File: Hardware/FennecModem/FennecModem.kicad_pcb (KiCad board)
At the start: 4 copper layers, 75 x 116.7 mm, 70 parts, among them J1 Conn_02x04_Odd_Even, J201 Conn_Coaxial, J3 Conn_02x04_Odd_Even, M1 Fan, Q2 AO3401A, Q3 MMBT3906, Q801 MMBT3904, U1 MCP6022, U2 L7805, U201 DRA818V, U4 SN74LVC245APW

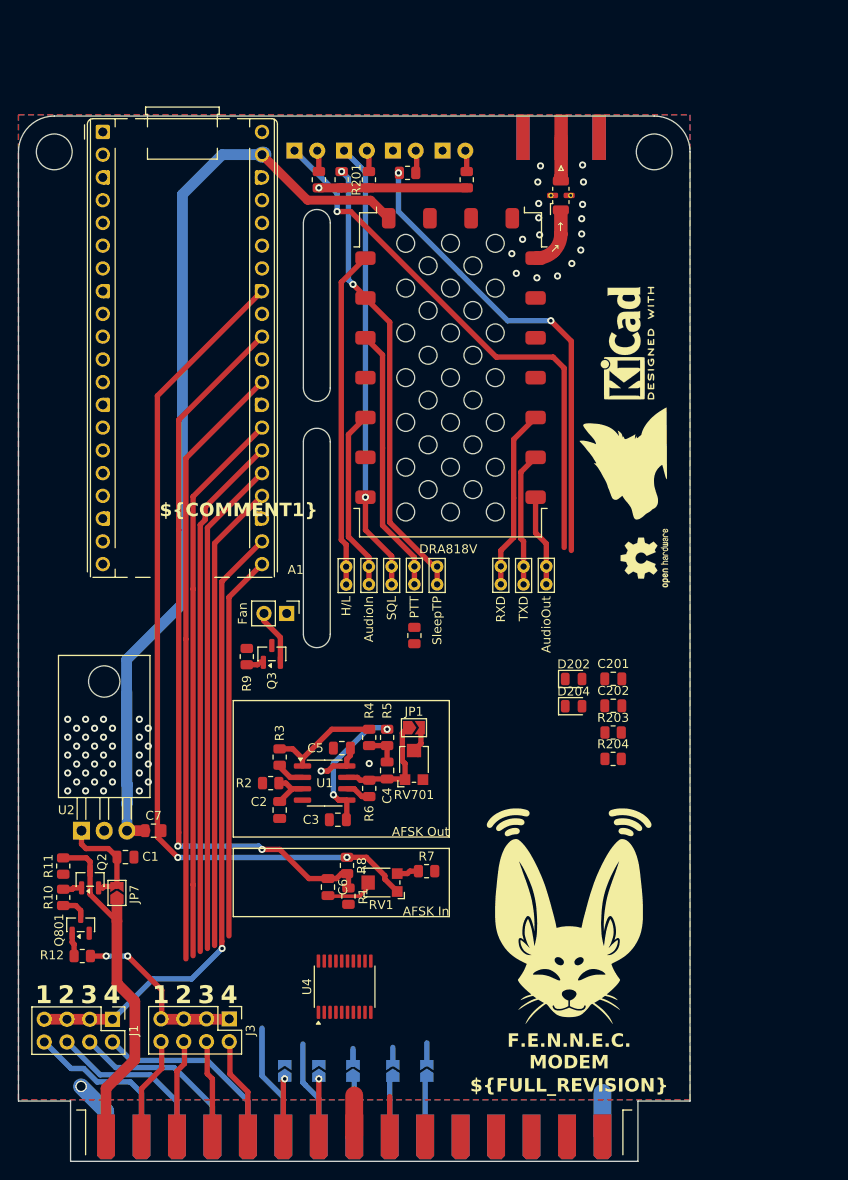
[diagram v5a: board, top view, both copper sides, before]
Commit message: Add all nets
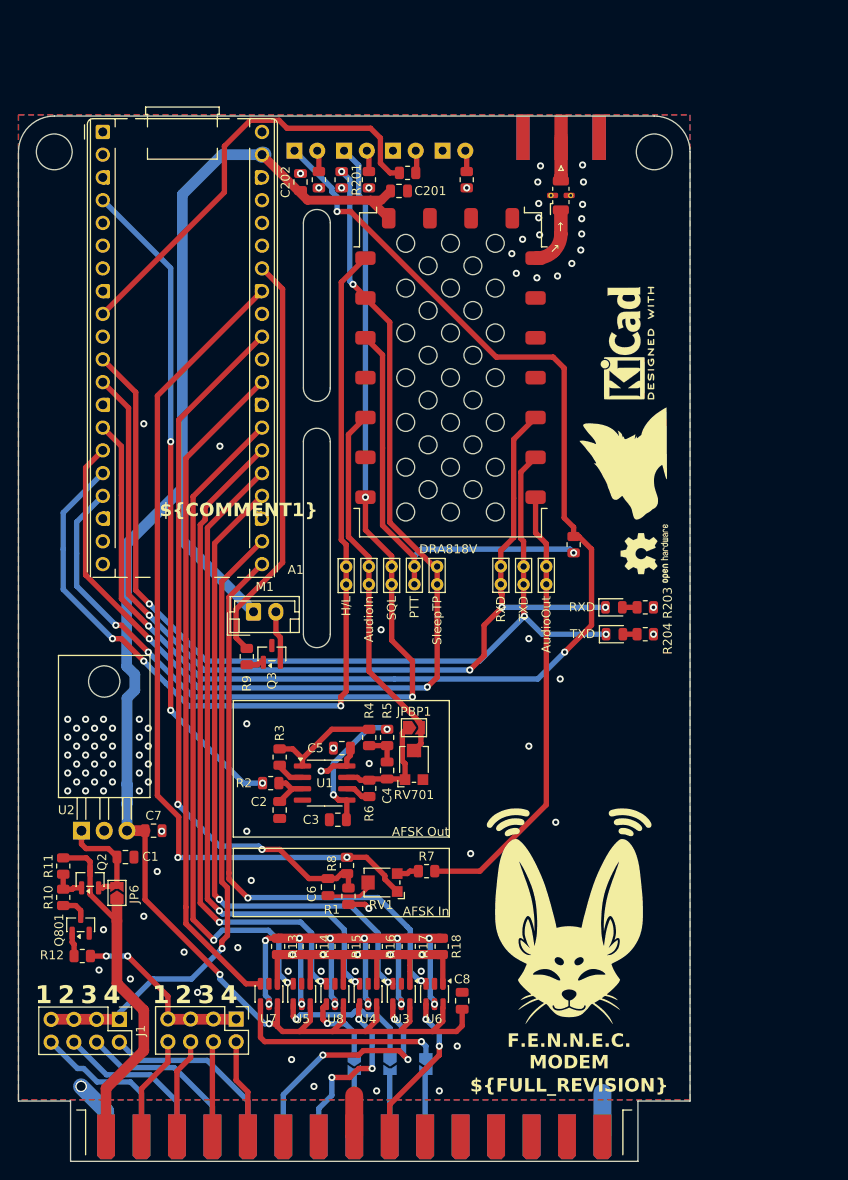
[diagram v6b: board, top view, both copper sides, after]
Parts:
- removed JP2: SolderJumper_2_Open, Jumper:SolderJumper-2_P1.3mm_Open_TrianglePad1.0x1.5mm
- removed the JP6 at (158.1, 146.8)
- added C8: 0.1μf, Capacitor_SMD:C_0805_2012Metric, F.Cu at (162.1, 138.9)
- added R13: 100K, Resistor_SMD:R_0805_2012Metric, F.Cu at (141.5, 132.9)
- added R14: 100K, Resistor_SMD:R_0805_2012Metric, F.Cu at (145.0, 132.9)
- added R15: 100K, Resistor_SMD:R_0805_2012Metric, F.Cu at (148.6, 132.9)
- added R16: 100K, Resistor_SMD:R_0805_2012Metric, F.Cu at (152.4, 132.9)
- added R17: 100K, Resistor_SMD:R_0805_2012Metric, F.Cu at (156.1, 132.9)
- added R18: 100K, Resistor_SMD:R_0805_2012Metric, F.Cu at (159.8, 132.9)
- added U3: SN74LVC1T45DBV, Package_TO_SOT_SMD:SOT-23-6, F.Cu at (155.3, 138.2)
- added U5: SN74LVC1T45DBV, Package_TO_SOT_SMD:SOT-23-6, F.Cu at (144.1, 138.2)
- added U6: SN74LVC1T45DBV, Package_TO_SOT_SMD:SOT-23-6, F.Cu at (159.0, 138.2)
- added U7: SN74LVC1T45DBV, Package_TO_SOT_SMD:SOT-23-6, F.Cu at (140.5, 138.2)
- added U8: SN74LVC1T45DBV, Package_TO_SOT_SMD:SOT-23-6, F.Cu at (147.8, 138.2)
- J1: value Conn_02x04_Odd_Even -> SEL_ADDR
- J3: value Conn_02x04_Odd_Even -> EN_ADDR
- M1: footprint Connector_PinHeader_2.54mm:PinHeader_1x02_P2.54mm_Vertical -> Connector_JST:JST_EH_B2B-EH-A_1x02_P2.50mm_Vertical
- U4: value SN74LVC245APW -> SN74LVC1T45DBV; footprint Package_SO:TSSOP-20_4.4x6.5mm_P0.65mm -> Package_TO_SOT_SMD:SOT-23-6
- moved C202 68.1 mm to (144.0, 47.5), turned to 90 degrees
- moved C201 59.5 mm to (155.0, 48.5)
- moved R206 20.5 mm to (174.5, 88.0), turned to -90 degrees
- moved R203 14.4 mm to (182.5, 95.0)
- moved R204 14.4 mm to (182.5, 98.0)
- moved D204 9.24 mm to (179.1, 98.0)
- moved D202 9.18 mm to (179.0, 95.0)
- moved JP4 4.21 mm to (154.0, 146.0), turned to -90 degrees
- moved JP3 4.03 mm to (150.0, 146.0), turned to -90 degrees
- moved JP5 3.78 mm to (158.0, 146.0), turned to -90 degrees
- moved M1 3.71 mm to (138.8, 95.5), turned to 0 degrees
- moved U4 2.75 mm to (151.6, 138.2), turned to -90 degrees
- moved J3 0.77 mm to (136.8, 141.0)
- moved J1 0.77 mm to (123.8, 141.0)
- moved REF** 0.50 mm to (182.5, 89.0)
- renumbered JP7 to JP6, JP1 to JPBP1
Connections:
- A1 pad 26: Net-(A1-GPIO20) -> /SPI2
- A1 pad 27: Net-(A1-GPIO21) -> /SPI3
- A1 pad 29: Net-(A1-GPIO22) -> /SPI4
- A1 pad 6: Net-(A1-GPIO4) -> /SDA
- A1 pad 7: Net-(A1-GPIO5) -> /SCL
- JP3 pad 1: /SDA -> /Backplane/_SPI_SDA2
- JP3 pad 2: Net-(A1-GPIO4) -> Net-(JP3-B)
- JP4 pad 1: /SPI2 -> /Backplane/_SPI_SDA3
- JP4 pad 2: Net-(A1-GPIO20) -> Net-(JP4-B)
- JP5 pad 1: /SPI3 -> /Backplane/_SPI_SDA4
- JP5 pad 2: Net-(A1-GPIO21) -> Net-(JP5-B)
- U302 pad 11: /SCL -> unconnected-(U302-I2C_SCL-Pad11)
- U302 pad 12: /SPI_CLK -> /Backplane/_SPI_CLK
- U302 pad 13: /SDA -> unconnected-(U302-I2C_SDA-Pad13)
- U302 pad 14: /SDI -> /Backplane/_SPI_SDA1
- U302 pad 16: /SPI2 -> Net-(JP3-B)
- U302 pad 17: /SDO -> /Backplane/_SPI_SDO
- U302 pad 18: /SPI3 -> Net-(JP4-B)
- U302 pad 20: /SPI4 -> Net-(JP5-B)
- U4 pad 1: unconnected-(U4-DIR-Pad1) -> +3.3V
- U4 pad 2: unconnected-(U4-A1-Pad2) -> GND
- U4 pad 3: unconnected-(U4-A2-Pad3) -> /SDI
- U4 pad 4: unconnected-(U4-A3-Pad4) -> /Backplane/_SPI_SDA1
- U4 pad 5: unconnected-(U4-A4-Pad5) -> /Backplane/DIR
- U4 pad 6: unconnected-(U4-A5-Pad6) -> +5V
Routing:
- net /RXD: track 15.0 -> 104.6 mm, vias 0 -> 3
- net /TXD: track 20.2 -> 109.4 mm, vias 0 -> 4
- net /PTT: track 61.4 -> 150.4 mm, vias 1 -> 3
- net +5V: track 116.2 -> 196.7 mm, vias 0 -> 2
- net /TONE_OUT: track 0.00 -> 73.7 mm, vias 0 -> 3
- net Net-(A1-GPIO22): track 70.3 -> 0.00 mm
- net /Sleep: track 50.7 -> 120.8 mm, vias 2 -> 4
- net /SPI3: track 6.78 -> 75.4 mm, vias 0 -> 2
- net /SPI4: track 6.72 -> 75.1 mm
- net /SQL: track 50.6 -> 118.1 mm, vias 1 -> 4
- net /SPI2: track 6.69 -> 73.9 mm, vias 0 -> 2
- net /Backplane/DIR: track 0.00 -> 67.0 mm, vias 0 -> 12
- net /H/L: track 37.8 -> 102.8 mm, vias 0 -> 3
- net Net-(A1-GPIO21): track 64.0 -> 0.00 mm
- net Net-(A1-GPIO20): track 60.6 -> 0.00 mm
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
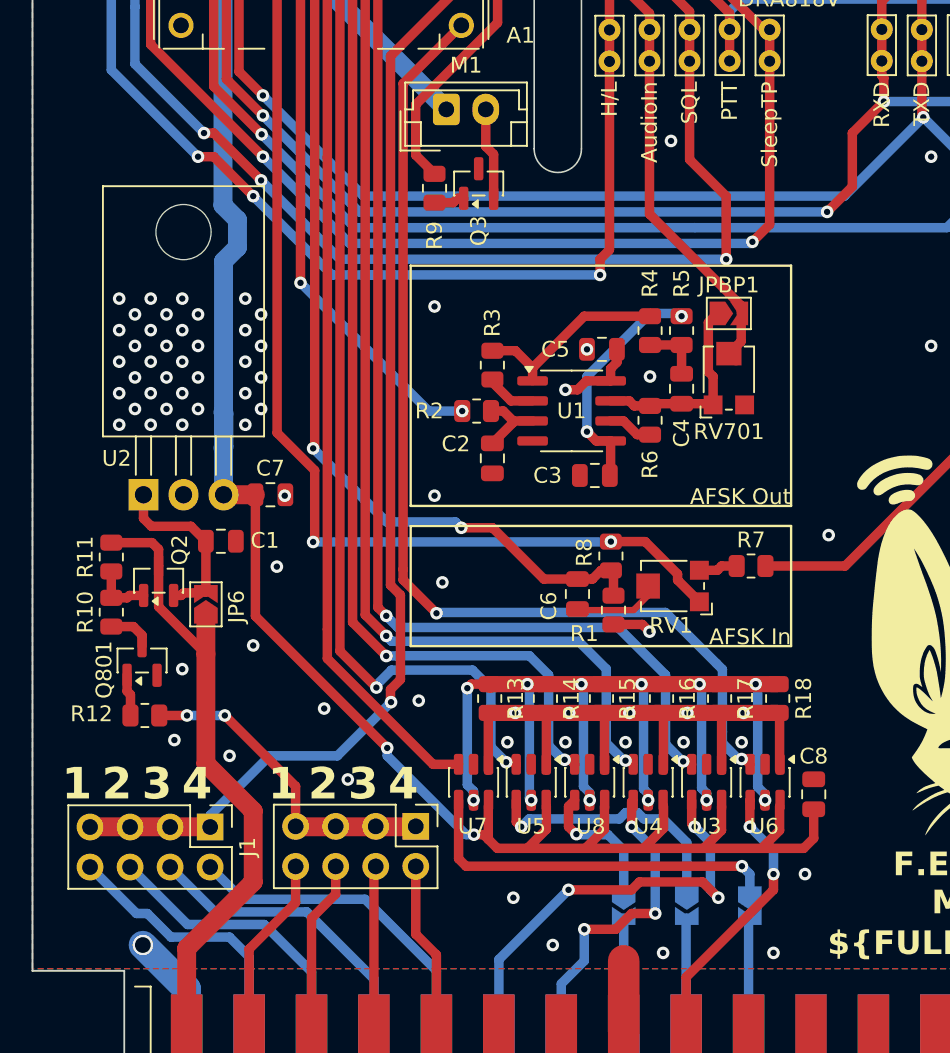
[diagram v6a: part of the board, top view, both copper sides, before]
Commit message: Implement new power supply
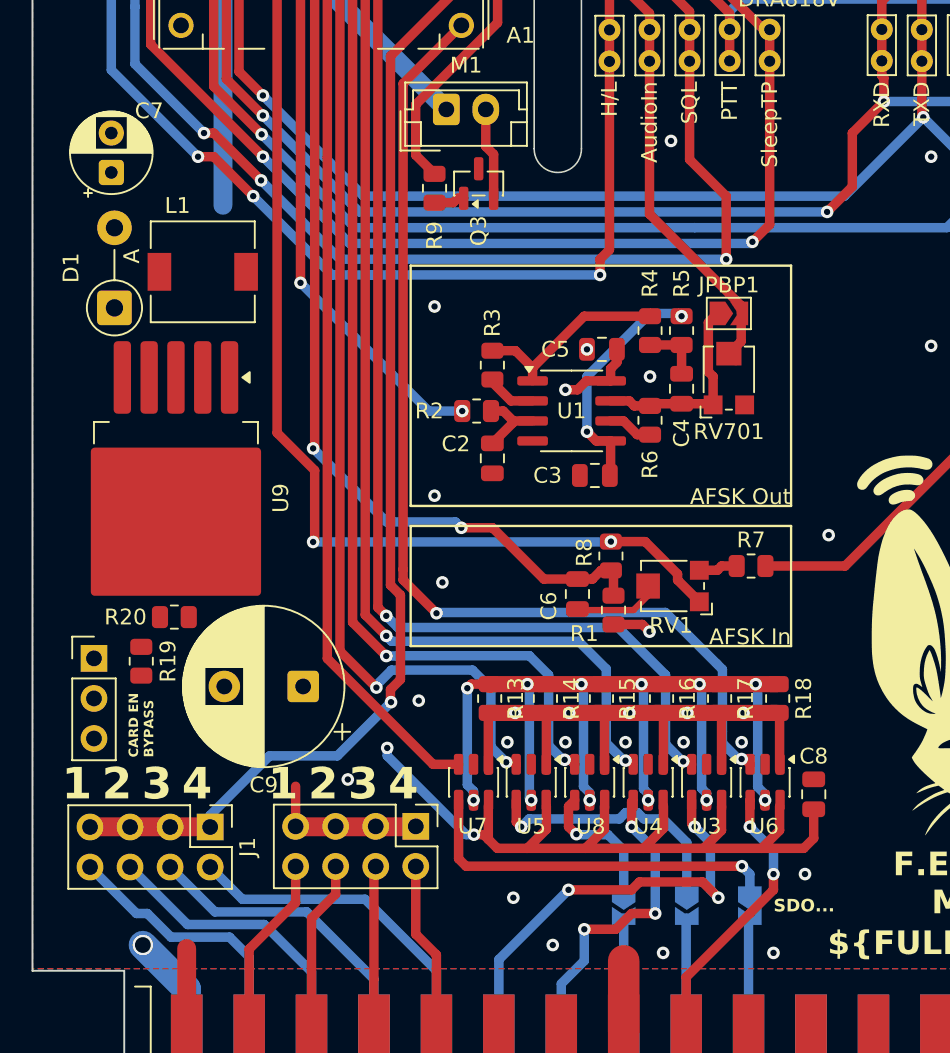
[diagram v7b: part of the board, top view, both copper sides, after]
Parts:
- removed C1: 10μf, Capacitor_SMD:C_0805_2012Metric
- removed JP6: SolderJumper_2_Open, Jumper:SolderJumper-2_P1.3mm_Open_TrianglePad1.0x1.5mm
- removed Q2: AO3401A, Package_TO_SOT_SMD:SOT-23
- removed Q801: MMBT3904, Package_TO_SOT_SMD:SOT-23
- removed R10, R12: 1K, Resistor_SMD:R_0805_2012Metric
- removed R11: 100K, Resistor_SMD:R_0805_2012Metric
- removed U2: L7805, Package_TO_SOT_THT:TO-220-3_Horizontal_TabDown
- added C9: 680uF, Capacitor_THT:CP_Radial_D10.0mm_P5.00mm, F.Cu at (129.7, 132.1)
- added D1: 1N5821, Diode_THT:D_DO-41_SOD81_P5.08mm_Vertical_AnodeUp, F.Cu at (117.7, 108.1)
- added J4: CARD_EN_BYPASS, Connector_PinHeader_2.54mm:PinHeader_1x03_P2.54mm_Vertical, F.Cu at (116.4, 130.3)
- added L1: 33uH, Inductor_SMD:L_6.3x6.3_H3, F.Cu at (123.3, 105.8)
- added R19: 1K, Resistor_SMD:R_0805_2012Metric, F.Cu at (119.4, 130.5)
- added R20: 10K, Resistor_SMD:R_0805_2012Metric, F.Cu at (121.5, 127.7)
- added U9: LM2596S-5, Package_TO_SOT_SMD:TO-263-5_TabPin3, F.Cu at (121.6, 120.2)
- C7: value 0.1μf -> 220uF; footprint Capacitor_SMD:C_0805_2012Metric -> Capacitor_THT:CP_Radial_D5.0mm_P2.50mm
- moved C7 22.8 mm to (117.5, 99.5), turned to 90 degrees
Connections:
- U302 pad 29: unconnected-(U302-UNUSED5-Pad29) -> +5VP
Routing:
- net +5V: track 196.7 -> 153.7 mm
- net +12V: track 40.6 -> 5.41 mm
- net Net-(JP6-B): track 11.4 -> 0.00 mm
- net /Backplane/CARD_EN: track 20.7 -> 10.2 mm, vias 2 -> 0
- net Net-(Q2-G): track 3.79 -> 0.00 mm
- net Net-(Q801-C): track 2.84 -> 0.00 mm
- net Net-(Q801-B): track 2.64 -> 0.00 mm
- net GND: vias 87 -> 44
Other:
- board text added: "CARD EN BYPASS"
- board text added: "SDO..."

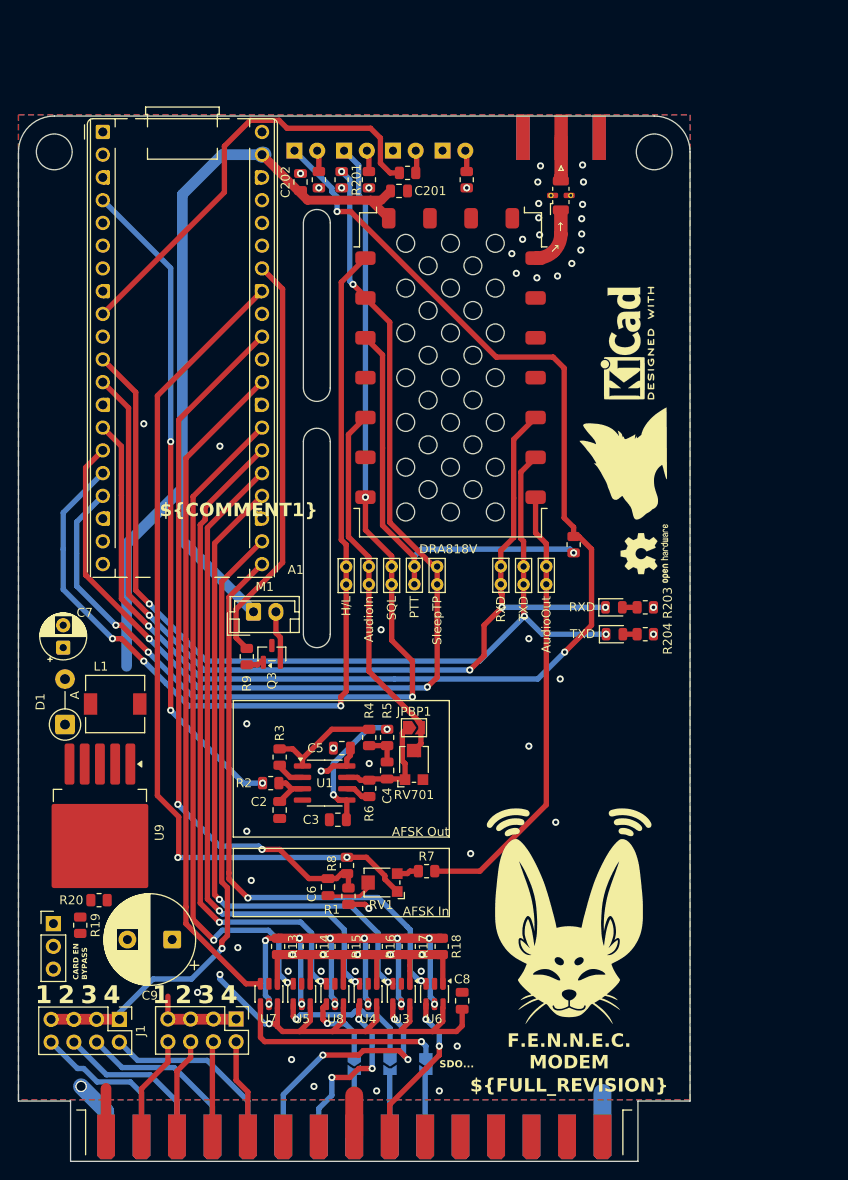
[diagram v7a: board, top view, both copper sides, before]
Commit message: Add new driver system
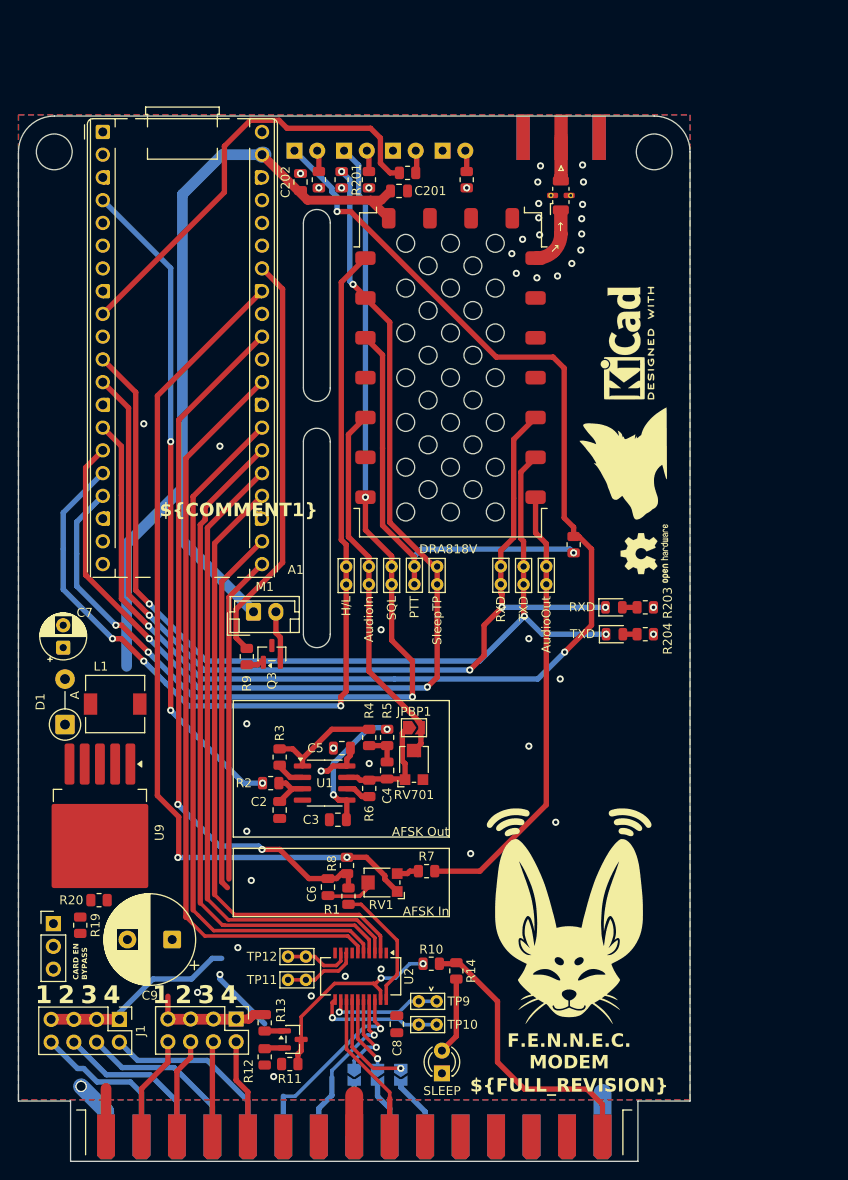
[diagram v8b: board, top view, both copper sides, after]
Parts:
- removed R15, R16, R17, R18: 100K, Resistor_SMD:R_0805_2012Metric
- removed U3, U4, U5, U6, U7, U8: SN74LVC1T45DBV, Package_TO_SOT_SMD:SOT-23-6
- added D2: SLEEP, LED_THT:LED_D3.0mm, F.Cu at (159.8, 147.0)
- added Q901: MMBT3904, Package_TO_SOT_SMD:SOT-23, F.Cu at (143.1, 143.2)
- added R10: 10k, Resistor_SMD:R_0805_2012Metric, F.Cu at (158.6, 134.8)
- added R11: 23k, Resistor_SMD:R_0805_2012Metric, F.Cu at (142.8, 146.0)
- added R12: 0R, Resistor_SMD:R_0805_2012Metric, F.Cu at (140.0, 145.2)
- added TP10: UNUSED_2_OUT, TestPoint:TestPoint_Bridge_Pitch2.0mm_Drill0.7mm, F.Cu at (159.2, 141.6)
- added TP11: UNUSED_1, TestPoint:TestPoint_Bridge_Pitch2.0mm_Drill0.7mm, F.Cu at (144.6, 136.6)
- added TP12: UNUSED_2, TestPoint:TestPoint_Bridge_Pitch2.0mm_Drill0.7mm, F.Cu at (144.6, 134.0)
- added TP9: UNUSED_1_OUT, TestPoint:TestPoint_Bridge_Pitch2.0mm_Drill0.7mm, F.Cu at (159.2, 139.0)
- added U2: SN74CBTLV3245A, Package_SO:SSOP-20_3.9x8.7mm_P0.635mm, F.Cu at (150.7, 136.2)
- R13: value 100K -> 1k
- R14: value 100K -> 2K
- moved R14 16.6 mm to (161.4, 135.6)
- moved R13 8.67 mm to (140.0, 141.4)
- moved C8 7.76 mm to (154.8, 141.6), turned to -90 degrees
- moved JP5 3.05 mm to (155.2, 147.2)
- moved JP4 1.84 mm to (152.6, 147.2)
- moved JP3 1.20 mm to (150.0, 147.2)
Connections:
- C8 pad 1: +5V -> +3.3V
- R13 pad 1: /Backplane/DIR -> /Backplane/CARD_EN
- R13 pad 2: +3.3V -> Net-(Q901-B)
- R14 pad 1: /Backplane/DIR -> +5VP
- R14 pad 2: +3.3V -> Net-(D2-A)
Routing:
- net /Backplane/DIR: track 67.0 -> 0.00 mm, vias 12 -> 0
- net +5V: track 153.7 -> 111.2 mm, vias 2 -> 1
- net +3.3V: track 56.5 -> 19.7 mm, vias 13 -> 7
- net +5VP: track 0.00 -> 32.4 mm
- net /SDO: track 66.3 -> 36.7 mm, vias 2 -> 0
- net Net-(Q901-C): track 0.00 -> 23.6 mm, vias 0 -> 2
- net Net-(U2-B8): track 0.00 -> 14.1 mm, vias 0 -> 1
- net Net-(U2-B7): track 0.00 -> 12.8 mm, vias 0 -> 1
- net /Backplane/_SPI_SDA4: track 23.9 -> 11.7 mm
- net /SPI4: track 75.1 -> 84.6 mm
- net Net-(D2-A): track 0.00 -> 8.66 mm
- net Net-(U2-A7): track 0.00 -> 8.45 mm
- net /Backplane/_SPI_SDA3: track 16.8 -> 8.59 mm
- net /CARD_SEL: track 70.7 -> 63.1 mm, vias 1 -> 0
- net Net-(U2-A8): track 0.00 -> 7.42 mm
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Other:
- board text removed: "SDO..."
